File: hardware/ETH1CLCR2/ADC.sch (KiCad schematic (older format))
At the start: 20 parts, among them U601 ADS8681PWR, U602 ADS8681PWR, U603 REF5040ID

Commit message: Project based on https://hackaday.io/project/165409-precision-impedance-meter-asdflcr1
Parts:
- removed C607, C608: C, symbol Device:C
- removed R609: 0R22, symbol Device:R
- removed U603: REF5040ID, Package_SO:SOIC-8_3.9x4.9mm_P1.27mm, symbol Reference_Voltage:REF5040ID
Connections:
- no-connect marks 3 -> 2
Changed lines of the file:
@@
 $Descr A4 11693 8268
 encoding utf-8
-Sheet 6 7
+Sheet 6 10
 Title ""
 Date ""
@@
 	6000 2350 6050 2350
 $Comp
-L Reference_Voltage:REF5040ID U603
-U 1 1 60A85CB4
-P 1450 5800
-F 0 "U603" H 1650 6150 50  0000 C CNN
-F 1 "REF5040ID" H 1650 6050 50  0000 C CNN
-F 2 "Package_SO:SOIC-8_3.9x4.9mm_P1.27mm" H 1375 5550 50  0001 L CIN
-F 3 "http://www.ti.com/lit/ds/symlink/ref5030.pdf" H 1400 5800 50  0001 C CIN
-	1    1450 5800
-	1    0    0    -1
-$EndComp
-$Comp
-L power:GND #PWR0617
-U 1 1 60A870C8
-P 1350 6350
-F 0 "#PWR0617" H 1350 6100 50  0001 C CNN
-F 1 "GND" H 1355 6177 50  0000 C CNN
-F 2 "" H 1350 6350 50  0001 C CNN
-F 3 "" H 1350 6350 50  0001 C CNN
-	1    1350 6350
-	1    0    0    -1
-$EndComp
-$Comp
-L power:+5V #PWR0615
-U 1 1 60A87F9A
-P 1350 5500
-F 0 "#PWR0615" H 1350 5350 50  0001 C CNN
-F 1 "+5V" H 1365 5673 50  0000 C CNN
-F 2 "" H 1350 5500 50  0001 C CNN
-F 3 "" H 1350 5500 50  0001 C CNN
-	1    1350 5500
-	1    0    0    -1
-$EndComp
-NoConn ~ 1050 5800
-$Comp
-L Device:C C607
-U 1 1 60A8909E
-P 1950 6200
-F 0 "C607" H 2065 6246 50  0000 L CNN
-F 1 "C" H 2065 6155 50  0000 L CNN
-F 2 "" H 1988 6050 50  0001 C CNN
-F 3 "~" H 1950 6200 50  0001 C CNN
-	1    1950 6200
-	1    0    0    -1
-$EndComp
-$Comp
-L Device:C C608
-U 1 1 60A8961B
-P 2450 6200
-F 0 "C608" H 2565 6246 50  0000 L CNN
-F 1 "C" H 2565 6155 50  0000 L CNN
-F 2 "" H 2488 6050 50  0001 C CNN
-F 3 "~" H 2450 6200 50  0001 C CNN
-	1    2450 6200
-	1    0    0    -1
-$EndComp
-Wire Wire Line
-	1950 5900 1850 5900
-$Comp
-L power:GND #PWR0618
-U 1 1 60A89D12
-P 1950 6350
-F 0 "#PWR0618" H 1950 6100 50  0001 C CNN
-F 1 "GND" H 1955 6177 50  0000 C CNN
-F 2 "" H 1950 6350 50  0001 C CNN
-F 3 "" H 1950 6350 50  0001 C CNN
-	1    1950 6350
-	1    0    0    -1
-$EndComp
-$Comp
-L power:GND #PWR0619
-U 1 1 60A89FD2
-P 2450 6350
-F 0 "#PWR0619" H 2450 6100 50  0001 C CNN
-F 1 "GND" H 2455 6177 50  0000 C CNN
-F 2 "" H 2450 6350 50  0001 C CNN
-F 3 "" H 2450 6350 50  0001 C CNN
-	1    2450 6350
-	1    0    0    -1
-$EndComp
-$Comp
-L Device:R R609
-U 1 1 60A8A3C7
-P 2450 5900
-F 0 "R609" H 2520 5946 50  0000 L CNN
-F 1 "0R22" H 2520 5855 50  0000 L CNN
-F 2 "" V 2380 5900 50  0001 C CNN
-F 3 "~" H 2450 5900 50  0001 C CNN
-	1    2450 5900
-	1    0    0    -1
-$EndComp
-Wire Wire Line
-	1850 5700 2450 5700
-Wire Wire Line
-	2450 5700 2450 5750
-Wire Wire Line
-	1950 5900 1950 6050
-Wire Wire Line
-	1350 6350 1350 6100
-$Comp
-L power:+4V #PWR0616
-U 1 1 60A8F8A5
-P 2450 5500
-F 0 "#PWR0616" H 2450 5350 50  0001 C CNN
-F 1 "+4V" H 2465 5673 50  0000 C CNN
-F 2 "" H 2450 5500 50  0001 C CNN
-F 3 "" H 2450 5500 50  0001 C CNN
-	1    2450 5500
-	1    0    0    -1
-$EndComp
-Wire Wire Line
-	2450 5500 2450 5700
-Connection ~ 2450 5700
-$Comp
 L power:+4V #PWR0604

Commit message: Schematic design
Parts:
- C601, C602: footprint (none) -> Capacitor_SMD:C_0603_1608Metric_Pad1.08x0.95mm_HandSolder
- R603, R606: value R -> 0
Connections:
- net ADC_VIN: now reaches R606.2
- net ADC_IIN: now reaches R603.2
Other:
- moved on the sheet: C603, C604, C605, C606, R607, R608
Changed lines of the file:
@@
 $Descr A4 11693 8268
 encoding utf-8
-Sheet 6 10
+Sheet 5 12
 Title ""
 Date ""
@@
 $EndComp
 Wire Wire Line
-	3400 5550 3400 5300
-Text Label 3400 5300 3    50   ~ 0
+	1100 6600 1100 6350
+Text Label 1100 6350 3    50   ~ 0
 CAP1
 $Comp
 L Device:R R607
 U 1 1 60AB2DE9
-P 3400 5700
-F 0 "R607" H 3470 5746 50  0000 L CNN
-F 1 "R" H 3470 5655 50  0000 L CNN
-F 2 "" V 3330 5700 50  0001 C CNN
-F 3 "~" H 3400 5700 50  0001 C CNN
-	1    3400 5700
+P 1100 6750
+F 0 "R607" H 1170 6796 50  0000 L CNN
+F 1 "R" H 1170 6705 50  0000 L CNN
+F 2 "" V 1030 6750 50  0001 C CNN
+F 3 "~" H 1100 6750 50  0001 C CNN
+	1    1100 6750
 	1    0    0    -1
 $EndComp
@@
 L Device:C C603
 U 1 1 60AB38E0
-P 3150 6100
-F 0 "C603" H 3265 6146 50  0000 L CNN
-F 1 "22u" H 3265 6055 50  0000 L CNN
-F 2 "" H 3188 5950 50  0001 C CNN
-F 3 "~" H 3150 6100 50  0001 C CNN
-	1    3150 6100
+P 850 7150
+F 0 "C603" H 965 7196 50  0000 L CNN
+F 1 "22u" H 965 7105 50  0000 L CNN
+F 2 "" H 888 7000 50  0001 C CNN
+F 3 "~" H 850 7150 50  0001 C CNN
+	1    850  7150
 	1    0    0    -1
 $EndComp
@@
 L Device:C C604
 U 1 1 60AB4823
-P 3650 6100
-F 0 "C604" H 3765 6146 50  0000 L CNN
-F 1 "1u" H 3765 6055 50  0000 L CNN
-F 2 "" H 3688 5950 50  0001 C CNN
-F 3 "~" H 3650 6100 50  0001 C CNN
-	1    3650 6100
-	1    0    0    -1
-$EndComp
-Wire Wire Line
-	3150 5950 3150 5900
-Wire Wire Line
-	3150 5900 3400 5900
-Wire Wire Line
-	3650 5900 3650 5950
-Wire Wire Line
-	3650 6250 3650 6300
-Wire Wire Line
-	3650 6300 3400 6300
-Wire Wire Line
-	3150 6300 3150 6250
-Wire Wire Line
-	3400 5850 3400 5900
-Connection ~ 3400 5900
-Wire Wire Line
-	3400 5900 3650 5900
+P 1350 7150
+F 0 "C604" H 1465 7196 50  0000 L CNN
+F 1 "1u" H 1465 7105 50  0000 L CNN
+F 2 "" H 1388 7000 50  0001 C CNN
+F 3 "~" H 1350 7150 50  0001 C CNN
+	1    1350 7150
+	1    0    0    -1
+$EndComp
+Wire Wire Line
+	850  7000 850  6950
+Wire Wire Line
+	850  6950 1100 6950
+Wire Wire Line
+	1350 6950 1350 7000
+Wire Wire Line
+	1350 7300 1350 7350
+Wire Wire Line
+	1350 7350 1100 7350
+Wire Wire Line
+	850  7350 850  7300
+Wire Wire Line
+	1100 6900 1100 6950
+Connection ~ 1100 6950
+Wire Wire Line
+	1100 6950 1350 6950
 $Comp
 L power:GND #PWR0620
 U 1 1 60AB7AF4
-P 3400 6350
-F 0 "#PWR0620" H 3400 6100 50  0001 C CNN
-F 1 "GND" H 3405 6177 50  0000 C CNN
-F 2 "" H 3400 6350 50  0001 C CNN
-F 3 "" H 3400 6350 50  0001 C CNN
-	1    3400 6350
-	1    0    0    -1
-$EndComp
-Wire Wire Line
-	3400 6350 3400 6300
-Connection ~ 3400 6300
-Wire Wire Line
-	3400 6300 3150 6300
-Wire Wire Line
-	4500 5550 4500 5300
-Text Label 4500 5300 3    50   ~ 0
+P 1100 7400
+F 0 "#PWR0620" H 1100 7150 50  0001 C CNN
+F 1 "GND" H 1105 7227 50  0000 C CNN
+F 2 "" H 1100 7400 50  0001 C CNN
+F 3 "" H 1100 7400 50  0001 C CNN
+	1    1100 7400
+	1    0    0    -1
+$EndComp
+Wire Wire Line
+	1100 7400 1100 7350
+Connection ~ 1100 7350
+Wire Wire Line
+	1100 7350 850  7350
+Wire Wire Line
+	2200 6600 2200 6350
+Text Label 2200 6350 3    50   ~ 0
 CAP2
 $Comp
 L Device:R R608
 U 1 1 60ABF713
-P 4500 5700
-F 0 "R608" H 4570 5746 50  0000 L CNN
-F 1 "R" H 4570 5655 50  0000 L CNN
-F 2 "" V 4430 5700 50  0001 C CNN
-F 3 "~" H 4500 5700 50  0001 C CNN
-	1    4500 5700
+P 2200 6750
+F 0 "R608" H 2270 6796 50  0000 L CNN
+F 1 "R" H 2270 6705 50  0000 L CNN
+F 2 "" V 2130 6750 50  0001 C CNN
+F 3 "~" H 2200 6750 50  0001 C CNN
+	1    2200 6750
 	1    0    0    -1
 $EndComp
@@
 L Device:C C605
 U 1 1 60ABF719
-P 4250 6100
-F 0 "C605" H 4365 6146 50  0000 L CNN
-F 1 "22u" H 4365 6055 50  0000 L CNN
-F 2 "" H 4288 5950 50  0001 C CNN
-F 3 "~" H 4250 6100 50  0001 C CNN
-	1    4250 6100
+P 1950 7150
+F 0 "C605" H 2065 7196 50  0000 L CNN
+F 1 "22u" H 2065 7105 50  0000 L CNN
+F 2 "" H 1988 7000 50  0001 C CNN
+F 3 "~" H 1950 7150 50  0001 C CNN
+	1    1950 7150
 	1    0    0    -1
 $EndComp
@@
 L Device:C C606
 U 1 1 60ABF71F
-P 4750 6100
-F 0 "C606" H 4865 6146 50  0000 L CNN
-F 1 "1u" H 4865 6055 50  0000 L CNN
-F 2 "" H 4788 5950 50  0001 C CNN
-F 3 "~" H 4750 6100 50  0001 C CNN
-	1    4750 6100
-	1    0    0    -1
-$EndComp
-Wire Wire Line
-	4250 5950 4250 5900
-Wire Wire Line
-	4250 5900 4500 5900
-Wire Wire Line
-	4750 5900 4750 5950
-Wire Wire Line
-	4750 6250 4750 6300
-Wire Wire Line
-	4750 6300 4500 6300
-Wire Wire Line
-	4250 6300 4250 6250
-Wire Wire Line
-	4500 5850 4500 5900
-Connection ~ 4500 5900
-Wire Wire Line
-	4500 5900 4750 5900
+P 2450 7150
+F 0 "C606" H 2565 7196 50  0000 L CNN
+F 1 "1u" H 2565 7105 50  0000 L CNN
+F 2 "" H 2488 7000 50  0001 C CNN
+F 3 "~" H 2450 7150 50  0001 C CNN
+	1    2450 7150
+	1    0    0    -1
+$EndComp
+Wire Wire Line
+	1950 7000 1950 6950
+Wire Wire Line
+	1950 6950 2200 6950
+Wire Wire Line
+	2450 6950 2450 7000
+Wire Wire Line
+	2450 7300 2450 7350
+Wire Wire Line
+	2450 7350 2200 7350
+Wire Wire Line
+	1950 7350 1950 7300
+Wire Wire Line
+	2200 6900 2200 6950
+Connection ~ 2200 6950
+Wire Wire Line
+	2200 6950 2450 6950
 $Comp
 L power:GND #PWR0621
 U 1 1 60ABF72E
-P 4500 6350
-F 0 "#PWR0621" H 4500 6100 50  0001 C CNN
-F 1 "GND" H 4505 6177 50  0000 C CNN
-F 2 "" H 4500 6350 50  0001 C CNN
-F 3 "" H 4500 6350 50  0001 C CNN
-	1    4500 6350
-	1    0    0    -1
-$EndComp
-Wire Wire Line
-	4500 6350 4500 6300
-Connection ~ 4500 6300
-Wire Wire Line
-	4500 6300 4250 6300
+P 2200 7400
+F 0 "#PWR0621" H 2200 7150 50  0001 C CNN
+F 1 "GND" H 2205 7227 50  0000 C CNN
+F 2 "" H 2200 7400 50  0001 C CNN
+F 3 "" H 2200 7400 50  0001 C CNN
+	1    2200 7400
+	1    0    0    -1
+$EndComp
+Wire Wire Line
+	2200 7400 2200 7350
+Connection ~ 2200 7350
+Wire Wire Line
+	2200 7350 1950 7350
 $Comp
 L Device:R R604
@@
 F 0 "C602" H 5615 4396 50  0000 L CNN
 F 1 "330p" H 5615 4305 50  0000 L CNN
-F 2 "" H 5538 4200 50  0001 C CNN
+F 2 "Capacitor_SMD:C_0603_1608Metric_Pad1.08x0.95mm_HandSolder" H 5538 4200 50  0001 C CNN
 F 3 "~" H 5500 4350 50  0001 C CNN
 	1    5500 4350
@@
 F 0 "C601" H 5615 2396 50  0000 L CNN
 F 1 "330p" H 5615 2305 50  0000 L CNN
-F 2 "" H 5538 2200 50  0001 C CNN
+F 2 "Capacitor_SMD:C_0603_1608Metric_Pad1.08x0.95mm_HandSolder" H 5538 2200 50  0001 C CNN
 F 3 "~" H 5500 2350 50  0001 C CNN
 	1    5500 2350
@@
 P 5300 4150
 F 0 "R606" V 5093 4150 50  0000 C CNN
-F 1 "R" V 5184 4150 50  0000 C CNN
+F 1 "0" V 5184 4150 50  0000 C CNN
 F 2 "" V 5230 4150 50  0001 C CNN
 F 3 "~" H 5300 4150 50  0001 C CNN
@@
 P 5300 2150
 F 0 "R603" V 5093 2150 50  0000 C CNN
-F 1 "R" V 5184 2150 50  0000 C CNN
+F 1 "0" V 5184 2150 50  0000 C CNN
 F 2 "" V 5230 2150 50  0001 C CNN
 F 3 "~" H 5300 2150 50  0001 C CNN
@@
 Text HLabel 9100 4450 2    50   Output ~ 0
 ADC_MISO
+Text HLabel 5050 2150 0    50   Input ~ 0
+ADC_IIN
+Wire Wire Line
+	5050 2150 5150 2150
+Text HLabel 5050 4150 0    50   Input ~ 0
+ADC_VIN
+Wire Wire Line
+	5050 4150 5150 4150
+$Comp
+L power:PWR_FLAG #FLG0502
+U 1 1 61EEB163
+P 2200 6350
+F 0 "#FLG0502" H 2200 6425 50  0001 C CNN
+F 1 "PWR_FLAG" H 2200 6523 50  0000 C CNN
+F 2 "" H 2200 6350 50  0001 C CNN
+F 3 "~" H 2200 6350 50  0001 C CNN
+	1    2200 6350
+	1    0    0    -1
+$EndComp
+$Comp
+L power:PWR_FLAG #FLG0501
+U 1 1 61EEB401
+P 1100 6350
+F 0 "#FLG0501" H 1100 6425 50  0001 C CNN
+F 1 "PWR_FLAG" H 1100 6523 50  0000 C CNN
+F 2 "" H 1100 6350 50  0001 C CNN
+F 3 "~" H 1100 6350 50  0001 C CNN
+	1    1100 6350
+	1    0    0    -1
+$EndComp
 $EndSCHEMATC

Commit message: Footprints assigned.
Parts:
- added C507, C508, C509, C510: 100n, Capacitor_SMD:C_0603_1608Metric_Pad1.08x0.95mm_HandSolder, symbol Device:C
- C503: renamed from C603; footprint (none) -> Capacitor_SMD:C_0805_2012Metric_Pad1.18x1.45mm_HandSolder
- C504: renamed from C604; footprint (none) -> Capacitor_SMD:C_0603_1608Metric_Pad1.08x0.95mm_HandSolder
- C505: renamed from C605; footprint (none) -> Capacitor_SMD:C_0805_2012Metric_Pad1.18x1.45mm_HandSolder
- C506: renamed from C606; footprint (none) -> Capacitor_SMD:C_0603_1608Metric_Pad1.08x0.95mm_HandSolder
- R501: renamed from R601; footprint (none) -> Resistor_SMD:R_0603_1608Metric_Pad0.98x0.95mm_HandSolder
- R502: renamed from R602; footprint (none) -> Resistor_SMD:R_0603_1608Metric_Pad0.98x0.95mm_HandSolder
- R503: renamed from R603; footprint (none) -> Resistor_SMD:R_0603_1608Metric_Pad0.98x0.95mm_HandSolder
- R504: renamed from R604; footprint (none) -> Resistor_SMD:R_0603_1608Metric_Pad0.98x0.95mm_HandSolder
- R505: renamed from R605; footprint (none) -> Resistor_SMD:R_0603_1608Metric_Pad0.98x0.95mm_HandSolder
- R506: renamed from R606; footprint (none) -> Resistor_SMD:R_0603_1608Metric_Pad0.98x0.95mm_HandSolder
- R507: renamed from R607; value R -> 0R22; footprint (none) -> Resistor_SMD:R_0603_1608Metric_Pad0.98x0.95mm_HandSolder
- R508: renamed from R608; value R -> 0R22; footprint (none) -> Resistor_SMD:R_0603_1608Metric_Pad0.98x0.95mm_HandSolder
- U501: renamed from U601; footprint (none) -> Package_SO:TSSOP-16_4.4x5mm_P0.65mm
- U502: renamed from U602; footprint (none) -> Package_SO:TSSOP-16_4.4x5mm_P0.65mm
- renumbered C601 to C501, C602 to C502
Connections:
- net +3V3: now also C509.1, C510.1
- net +5V: now also C507.1, C508.1
- net GND: now also C507.2, C508.2, C509.2, C510.2

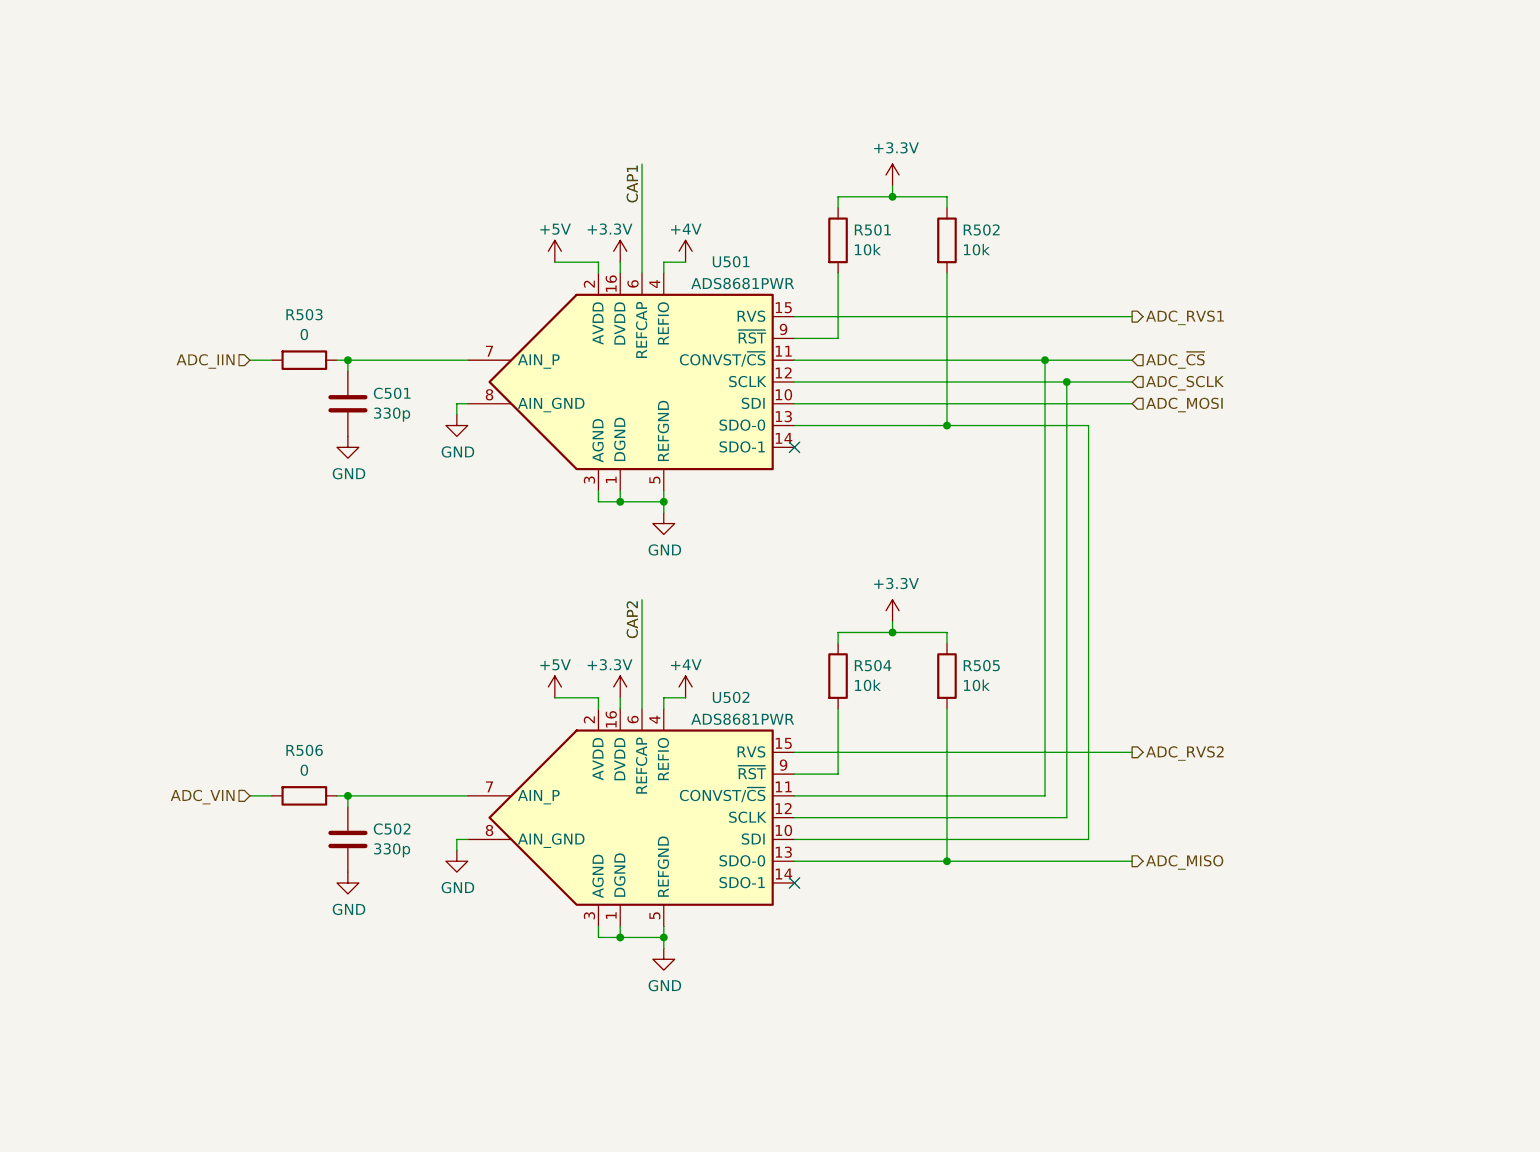
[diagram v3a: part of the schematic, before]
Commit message: Modification of the function generator schematic.
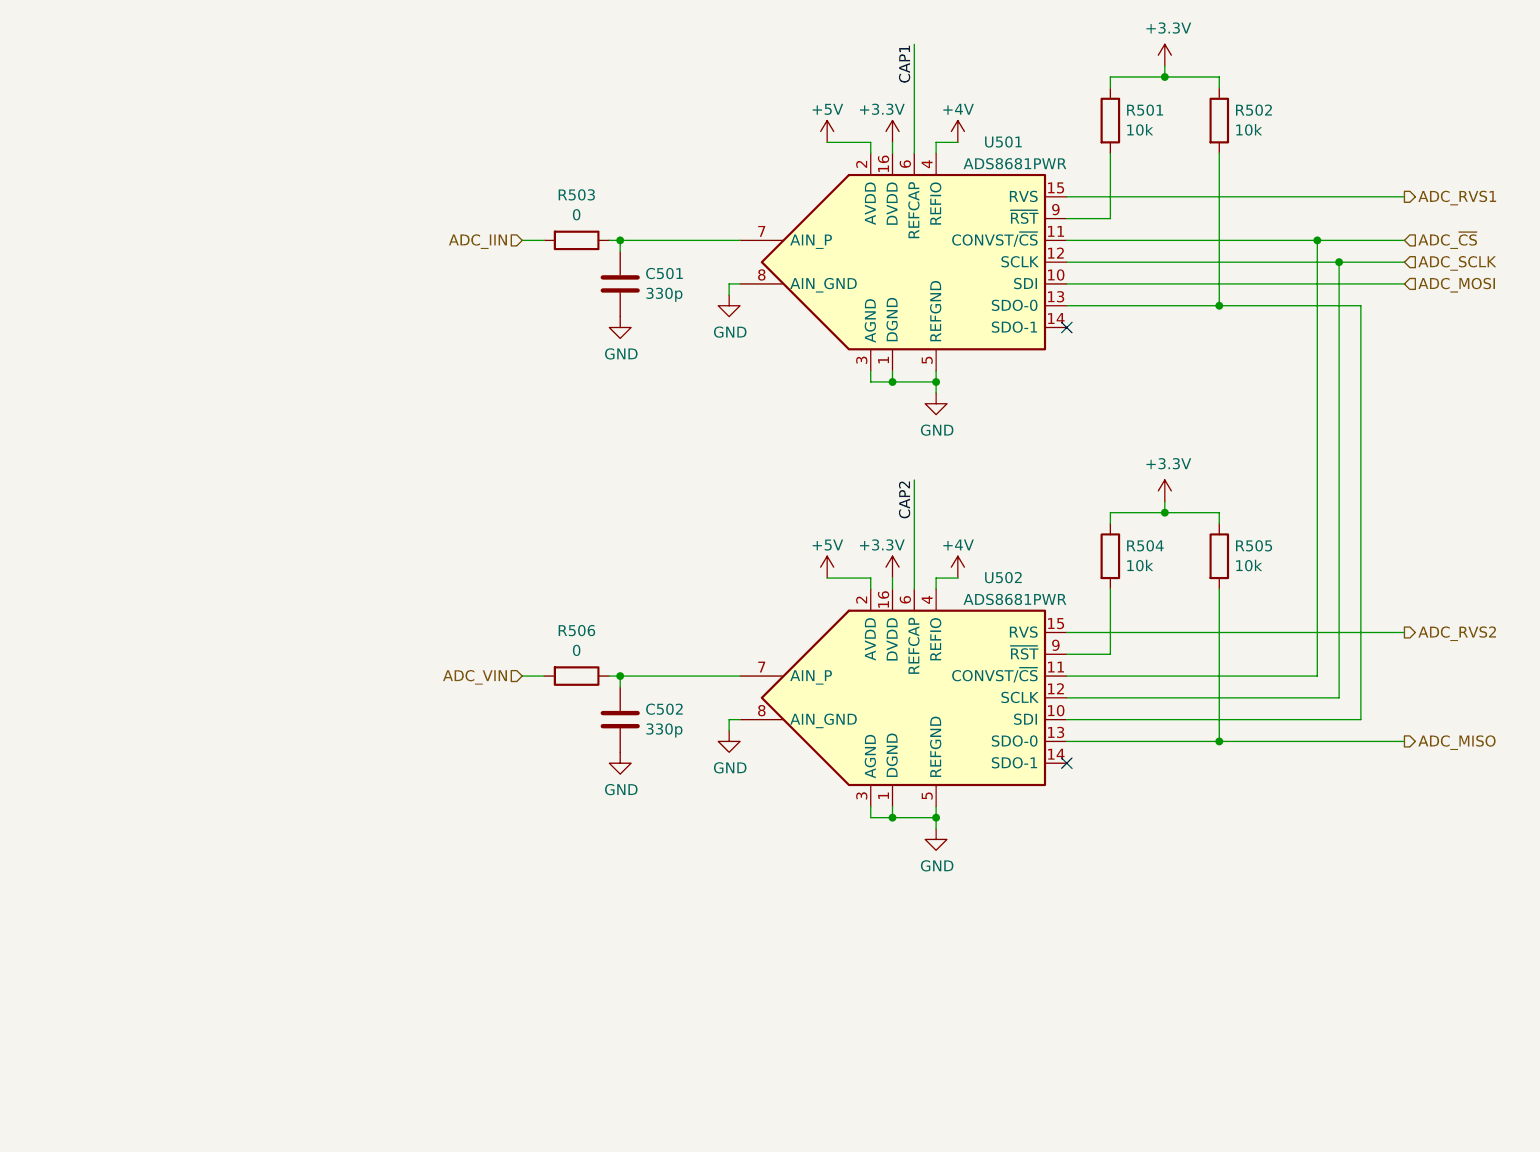
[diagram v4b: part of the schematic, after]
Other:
- moved on the sheet: C501, C502, R501, R502, R503, R504, R505, R506, U501, U502
